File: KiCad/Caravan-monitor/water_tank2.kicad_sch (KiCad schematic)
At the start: 3 parts, among them J4 Coolant temp

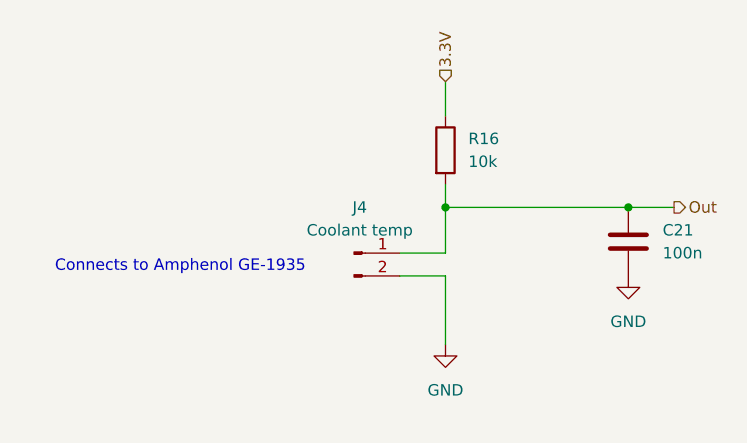
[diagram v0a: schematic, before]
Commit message: Display schematics
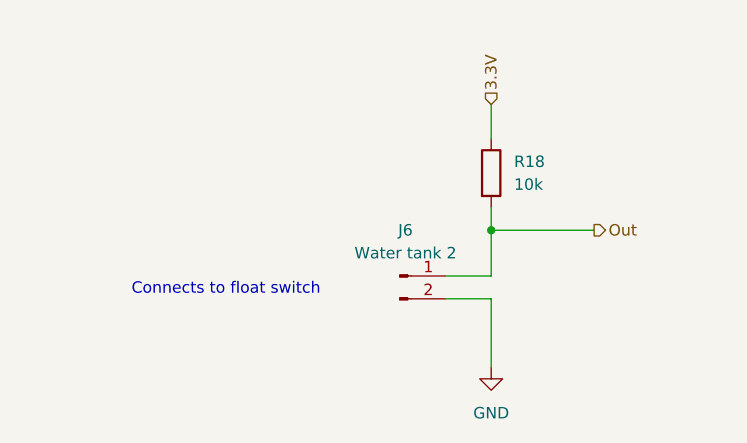
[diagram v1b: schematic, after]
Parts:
- removed C21: 100n, Capacitor_SMD:C_0805_2012Metric_Pad1.18x1.45mm_HandSolder, symbol Device:C
- removed J4: Coolant temp, Connector_JST:JST_XH_S2B-XH-A-1_1x02_P2.50mm_Horizontal, symbol Connector:Conn_01x02_Pin
- removed R16: 10k, Resistor_SMD:R_0805_2012Metric_Pad1.20x1.40mm_HandSolder, symbol Device:R
- added J6: Water tank 2, Connector_JST:JST_XH_S2B-XH-A-1_1x02_P2.50mm_Horizontal, symbol Connector:Conn_01x02_Pin
- added R18: 10k, Resistor_SMD:R_0805_2012Metric_Pad1.20x1.40mm_HandSolder, symbol Device:R
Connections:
- net 3.3V: now also R18.1
- net GND: now also J6.2 (Pin_2)
- net Out: now also J6.1 (Pin_1), R18.2
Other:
- note added: "Connects to float switch"
- note removed: "Connects to Amphenol GE-1935"

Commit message: Schematics done
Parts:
- R18: footprint Resistor_SMD:R_0805_2012Metric_Pad1.20x1.40mm_HandSolder -> Resistor_SMD:R_0402_1005Metric_Pad0.72x0.64mm_HandSolder
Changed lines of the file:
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@@
 			)
 		)
-		(property "Footprint" "Resistor_SMD:R_0805_2012Metric_Pad1.20x1.40mm_HandSolder"
+		(property "Footprint" "Resistor_SMD:R_0402_1005Metric_Pad0.72x0.64mm_HandSolder"
 			(at 145.542 87.63 90)
 			(effects

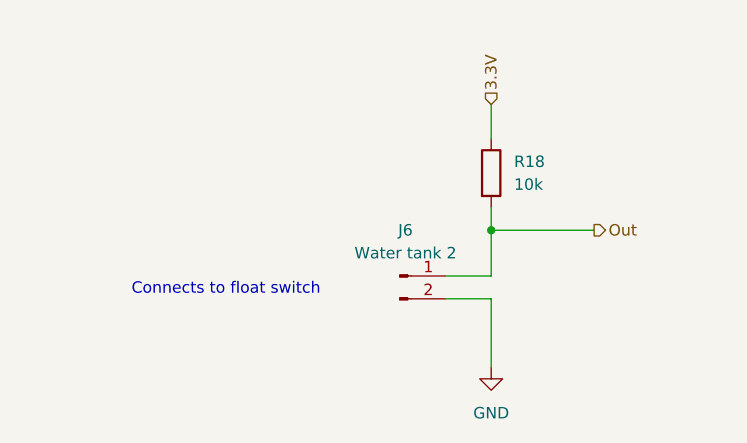
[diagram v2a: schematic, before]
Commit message: Schematic updates
Parts changed for JLCPCB assembly compatibility
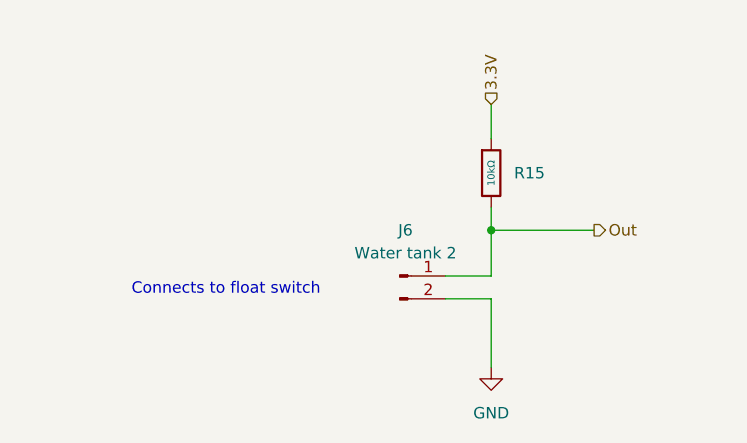
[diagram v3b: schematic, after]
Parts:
- removed R18: 10k, Resistor_SMD:R_0402_1005Metric_Pad0.72x0.64mm_HandSolder, symbol Device:R
- added R15: 10kΩ, PCM_JLCPCB:R_0402, symbol PCM_JLCPCB-Resistors:0402,10kΩ
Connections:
- net 3.3V: now also R15.1
- net Out: now also R15.2
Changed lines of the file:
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@@
 	)
 	(symbol
-		(lib_id "Device:R")
+		(lib_id "PCM_JLCPCB-Resistors:0402,10kΩ")
 		(at 147.32 87.63 0)
 		(unit 1)
@@
 		(dnp no)
 		(fields_autoplaced yes)
-		(property "Reference" "R18"
-			(at 149.86 86.3599 0)
+		(property "Reference" "R15"
+			(at 149.86 87.6299 0)
 			(effects
 				(font
@@
 			)
 		)
-		(property "Value" "10k"
-			(at 149.86 88.8999 0)
-			(effects
-				(font
-					(size 1.27 1.27)
-				)
-				(justify left)
-			)
-		)
-		(property "Footprint" "Resistor_SMD:R_0402_1005Metric_Pad0.72x0.64mm_HandSolder"
+		(property "Value" "10kΩ"
+			(at 147.32 87.63 90)
+			(do_not_autoplace yes)
+			(effects
+				(font
+					(size 0.8 0.8)
+				)
+			)
+		)
+		(property "Footprint" "PCM_JLCPCB:R_0402"
 			(at 145.542 87.63 90)
 			(effects
@@
 			)
 		)
-		(property "Datasheet" "~"
-			(at 147.32 87.63 0)
-			(effects
-				(font
-					(size 1.27 1.27)
-				)
-				(hide yes)
-			)
-		)
-		(property "Description" "Resistor"
-			(at 147.32 87.63 0)
-			(effects
-				(font
-					(size 1.27 1.27)
-				)
-				(hide yes)
-			)
+		(property "Datasheet" "https://www.lcsc.com/datasheet/lcsc_datasheet_2411221126_UNI-ROYAL-Uniroyal-Elec-0402WGF1002TCE_C25744.pdf"
+			(at 147.32 87.63 0)
+			(effects
+				(font
+					(size 1.27 1.27)
+				)
+				(hide yes)
+			)
+		)
+		(property "Description" "62.5mW Thick Film Resistors 50V ±100ppm/°C ±1% 10kΩ 0402 Chip Resistor - Surface Mount ROHS"
+			(at 147.32 87.63 0)
+			(effects
+				(font
+					(size 1.27 1.27)
+				)
+				(hide yes)
+			)
+		)
+		(property "LCSC" "C25744"
+			(at 147.32 87.63 0)
+			(effects
+				(font
+					(size 1.27 1.27)
+				)
+				(hide yes)
+			)
+		)
+		(property "Stock" "24372091"
+			(at 147.32 87.63 0)
+			(effects
+				(font
+					(size 1.27 1.27)
+				)
+				(hide yes)
+			)
+		)
+		(property "Price" "0.004USD"
+			(at 147.32 87.63 0)
+			(effects
+				(font
+					(size 1.27 1.27)
+				)
+				(hide yes)
+			)
+		)
+		(property "Process" "SMT"
+			(at 147.32 87.63 0)
+			(effects
+				(font
+					(size 1.27 1.27)
+				)
+				(hide yes)
+			)
+		)
+		(property "Minimum Qty" "20"
+			(at 147.32 87.63 0)
+			(effects
+				(font
+					(size 1.27 1.27)
+				)
+				(hide yes)
+			)
+		)
+		(property "Attrition Qty" "10"
+			(at 147.32 87.63 0)
+			(effects
+				(font
+					(size 1.27 1.27)
+				)
+				(hide yes)
+			)
+		)
+		(property "Class" "Basic Component"
+			(at 147.32 87.63 0)
+			(effects
+				(font
+					(size 1.27 1.27)
+				)
+				(hide yes)
+			)
+		)
+		(property "Category" "Resistors,Chip Resistor - Surface Mount"
+			(at 147.32 87.63 0)
+			(effects
+				(font
+					(size 1.27 1.27)
+				)
+				(hide yes)
+			)
+		)
+		(property "Manufacturer" "UNI-ROYAL(Uniroyal Elec)"
+			(at 147.32 87.63 0)
+			(effects
+				(font
+					(size 1.27 1.27)
+				)
+				(hide yes)
+			)
+		)
+		(property "Part" "0402WGF1002TCE"
+			(at 147.32 87.63 0)
+			(effects
+				(font
+					(size 1.27 1.27)
+				)
+				(hide yes)
+			)
+		)
+		(property "Resistance" "10kΩ"
+			(at 147.32 87.63 0)
+			(effects
+				(font
+					(size 1.27 1.27)
+				)
+				(hide yes)
+			)
+		)
+		(property "Power(Watts)" "62.5mW"
+			(at 147.32 87.63 0)
+			(effects
+				(font
+					(size 1.27 1.27)
+				)
+				(hide yes)
+			)
+		)
+		(property "Type" "Thick Film Resistors"
+			(at 147.32 87.63 0)
+			(effects
+				(font
+					(size 1.27 1.27)
+				)
+				(hide yes)
+			)
+		)
+		(property "Overload Voltage (Max)" "50V"
+			(at 147.32 87.63 0)
+			(effects
+				(font
+					(size 1.27 1.27)
+				)
+				(hide yes)
+			)
+		)
+		(property "Operating Temperature Range" "-55°C~+155°C"
+			(at 147.32 87.63 0)
+			(effects
+				(font
+					(size 1.27 1.27)
+				)
+				(hide yes)
+			)
+		)
+		(property "Tolerance" "±1%"
+			(at 147.32 87.63 0)
+			(effects
+				(font
+					(size 1.27 1.27)
+				)
+				(hide yes)
+			)
+		)
+		(property "Temperature Coefficient" "±100ppm/°C"
+			(at 147.32 87.63 0)
+			(effects
+				(font
+					(size 1.27 1.27)
+				)
+				(hide yes)
+			)
+		)
+		(pin "1"
 		)
 		(pin "2"
 		)
-		(pin "1"
-		)
 		(instances
-			(project "Caravan-monitor"
+			(project ""
 				(path "/4b94aa5f-1c73-4d2e-8117-e53a25103462/851f2a24-5658-4162-92c4-0233905600df"
-					(reference "R18")
+					(reference "R15")
 					(unit 1)
 				)
